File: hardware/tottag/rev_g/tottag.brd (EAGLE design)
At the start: 68.1 x 39.6 mm, 200 parts, among them J1 USB4110-GF-A, J2 DM3AT-SF-PEJM5, J3 TC2030-JLINK-NL-2SIDE, J4 TC2030-JLINK-NL-2SIDE, J5 MOLEX-PICO-SPOX-3SIDE, Q1 CSD75207W15, Q4 CSD75207W15, T1 HHM1595A1, U1 DW1000, U10 STM32F091CC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

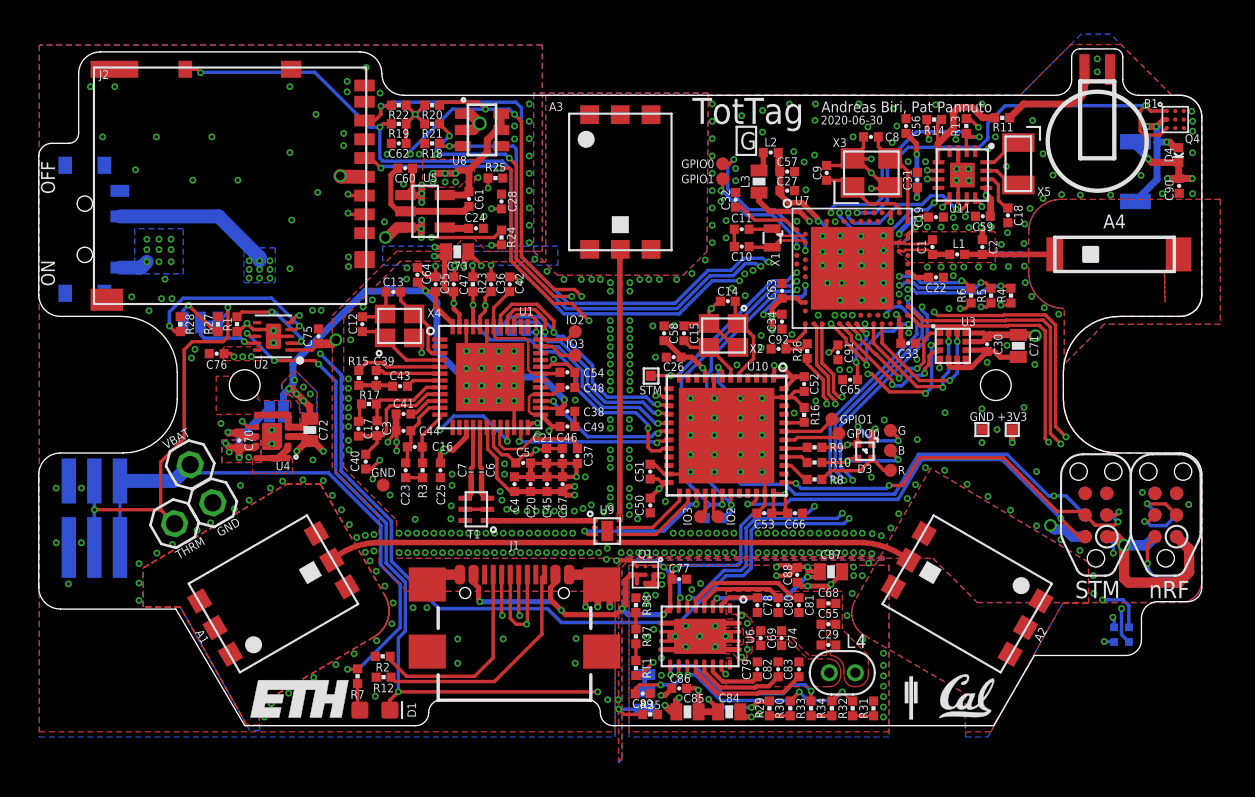
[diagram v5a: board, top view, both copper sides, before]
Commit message: rev_g: renumber R
This script will relabel parts as follows:

R26 : 4.7   0402_RES           => R1 : 4.7   0402_RES

R31 : 97.6   0402_RES          => R2 : 97.6   0402_RES
R32 : 97.6   0402_RES          => R3 : 97.6   0402_RES

R33 : 162   0402_RES           => R4 : 162   0402_RES
R34 : 162   0402_RES           => R5 : 162   0402_RES

R3 : 270   0402_RES            => R6 : 270   0402_RES

R4 : 470   0402_RES            => R7 : 470   0402_RES
R5 : 470   0402_RES            => R8 : 470   0402_RES
R6 : 470   0402_RES            => R9 : 470   0402_RES

R7 : 1k   0402_RES             => R10 : 1k   0402_RES
R8 : 1k   0402_RES             => R11 : 1k   0402_RES
R9 : 1k   0402_RES             => R12 : 1k   0402_RES
R10 : 1k   0402_RES            => R13 : 1k   0402_RES
R37 : 1k   0402_RES            => R14 : 1k   0402_RES
R38 : 1k   0402_RES            => R15 : 1k   0402_RES

R11 : 1.41k   0402_RES         => R16 : 1.41k   0402_RES

R1 : 2.2k   0402_RES           => R17 : 2.2k   0402_RES

R2 : 5.1k   0402_RES           => R18 : 5.1k   0402_RES
R12 : 5.1k   0402_RES          => R19 : 5.1k   0402_RES

R13 : 10k   0402_RES           => R20 : 10k   0402_RES
R27 : 10k   0402_RES           => R21 : 10k   0402_RES
R29 : 10k   0402_RES           => R22 : 10k   0402_RES
R30 : 10k   0402_RES           => R23 : 10k   0402_RES
R35 : 10k   0402_RES           => R24 : 10k   0402_RES

R15 : 11k   0402_RES           => R25 : 11k   0402_RES
R16 : 11k   0402_RES           => R26 : 11k   0402_RES

R17 : 16k   0402_RES           => R27 : 16k   0402_RES

R18 : 100k   0402_RES          => R28 : 100k   0402_RES
R19 : 100k   0402_RES          => R29 : 100k   0402_RES
R20 : 100k   0402_RES          => R30 : 100k   0402_RES
R21 : 100k   0402_RES          => R31 : 100k   0402_RES
R22 : 100k   0402_RES          => R32 : 100k   0402_RES
R23 : 100k   0402_RES          => R33 : 100k   0402_RES
R14 : 100k   0402_RES          => R34 : 100k   0402_RES

R24 : 3.3M   0402_RES          => R35 : 3.3M   0402_RES
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
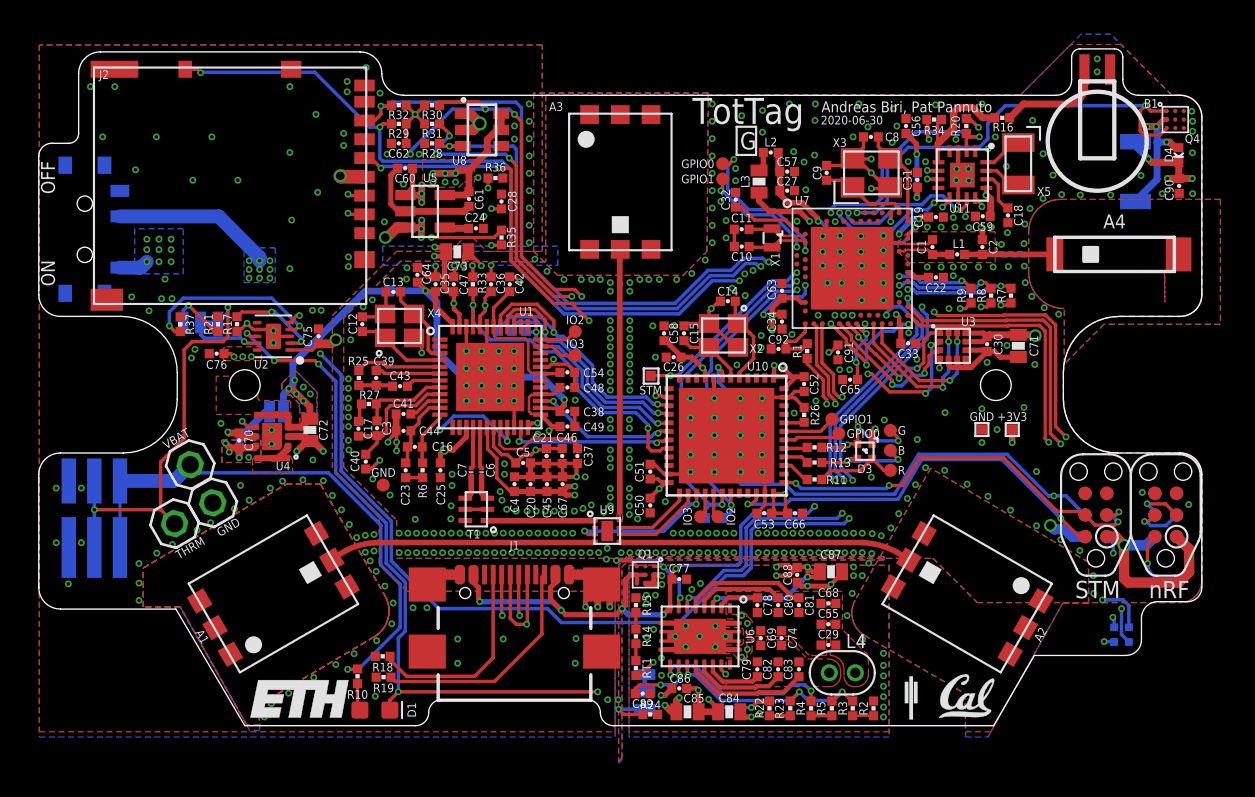
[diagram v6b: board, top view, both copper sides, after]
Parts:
- removed R38: 1k, passives:0402_RES
- added R36: 10M, passives:0402_RES
- R1: value 2.2k -> 4.7
- R11: value 1.41k -> 1k
- R12: value 5.1k -> 1k
- R13: value 10k -> 1k
- R14: value 100k -> 1k
- R15: value 11k -> 1k
- R16: value 11k -> 1.41k
- R17: value 16k -> 2.2k
- R18, R19: value 100k -> 5.1k
- R2: value 5.1k -> 97.6
- R20, R21, R22, R23: value 100k -> 10k
- R24: value 3.3M -> 10k
- R25: value 10M -> 11k
- R26: value 4.7 -> 11k
- R27: value 10k -> 16k
- R28: value DNP -> 100k
- R29, R30: value 10k -> 100k
- R3: value 270 -> 97.6
- R31, R32: value 97.6 -> 100k
- R33, R34: value 162 -> 100k
- R35: value 10k -> 3.3M
- R37: value 1k -> DNP
- R4, R5: value 470 -> 162
- R6: value 470 -> 270
- R7, R8, R9: value 1k -> 470
- moved R7 44.3 mm to (22.9, 18.7), turned to 90 degrees
- moved R32 44.2 mm to (-13.0, 29.9), turned to 0 degrees
- moved R31 42.9 mm to (-11.0, 28.8), turned to 180 degrees
- moved R22 41.5 mm to (8.74, -5.44), turned to 270 degrees
- moved R30 41.1 mm to (-11.0, 29.9), turned to 180 degrees
- moved R29 40.5 mm to (-13.0, 28.8), turned to 0 degrees
- moved R34 35.0 mm to (18.4, 29.1), turned to 180 degrees
- moved R14 35.0 mm to (0.91, -1.22), turned to 270 degrees
- moved R6 33.7 mm to (-11.6, 8.51), turned to 270 degrees
- moved R1 33.4 mm to (10.9, 15.5)
- moved R19 32.4 mm to (-13.9, -3.61), turned to 180 degrees
- moved R37 32.4 mm to (-25.8, 17.1)
- moved R33 31.8 mm to (-8.64, 19.4)
- moved R20 31.3 mm to (20.3, 28.7), turned to 90 degrees
- moved R23 31.0 mm to (9.96, -5.44), turned to 90 degrees
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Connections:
- net !NRF_CS_RTC: now also R34.2; no longer R14.2
- net !NRF_CS_SD: now also R31.1; no longer R21.1
- net !SD_DETECT: now also R29.1; no longer R19.1
- net BATIN: now also R35.1, R36.2; no longer R24.1, R25.2
- net BQ_FOD: now also R23.2, R3.1, R5.2; no longer R30.2, R32.1, R34.2
- net BQ_ILM: now also R4.1; no longer R33.1
- net BQ_RECT: now also R22.1; no longer R29.1
- net DW_IRQ: now also R33.2; no longer R23.2
- net GND: now also R17.1, R19.2, R20.2, R21.1, R24.1, R26.2, R28.2, R33.1, R36.1, R37.1; no longer R1.1, R12.2, R13.2, R16.2, R23.1, R27.1, R28.1, R31.2, R35.1, R38.1
- net LED_BLUE: now also R13.2; no longer R10.2
- net LED_GREEN: now also R12.2; no longer R9.2
- net LED_NRF_BLUE: now also R9.2; no longer R6.2
- net LED_NRF_GREEN: now also R8.2; no longer R5.2
- net LED_NRF_RED: now also R7.2; no longer R4.2
- net LED_RED: now also R11.2; no longer R8.2
- net N$1: now also R19.1; no longer R12.1
- net N$12: now also R27.2; no longer R17.2
- net N$13: now also R18.1; no longer R2.1
- net N$14: now also R6.1; no longer R3.1
- net N$16: now also R27.1; no longer R17.1
- net N$21: now also R25.2; no longer R15.2
- net N$22: now also R26.1; no longer R16.1
- net N$23: now also R12.1; no longer R9.1
- net N$24: now also R13.1; no longer R10.1
- net N$25: now also R11.1; no longer R8.1
- net N$28: now also R2.1, R3.2; no longer R31.1, R32.2
- net N$34: now also R17.2; no longer R1.2
- net N$45: now also R16.2; no longer R11.2
- net N$47: now also R21.2; no longer R27.2
- net N$49: now also R37.2; no longer R28.2
- net N$54: now also R10.2; no longer R7.2
- net N$59: now also R7.1; no longer R4.1
- net N$60: now also R8.1; no longer R5.1
- net N$61: now also R9.1; no longer R6.1
- net N$64: now also R22.2, R23.1; no longer R29.2, R30.1
- net N$66: now also R4.2, R5.1; no longer R33.2, R34.1
- net N$67: now also R24.2; no longer R35.2
- net N$69: now also R14.2; no longer R37.2
- net N$70: now also R14.1, R15.2; no longer R37.1, R38.2
- net N$8: now also R6.2; no longer R3.2
- net NRF_MISO: now also R32.1; no longer R22.1
- net NRF_MOSI: now also R30.1; no longer R20.1
- net RTC_WDI: now also R20.1; no longer R13.1
- net SD_EN: now also R28.1; no longer R18.1
- net VBAT: now also R10.1, R35.2; no longer R24.2, R7.1
- net VBAT_RTC: now also R16.1, R34.1; no longer R11.1, R14.1
- net VCC_SDCARD: now also R29.2, R30.2, R31.2, R32.2; no longer R19.2, R20.2, R21.2, R22.2
- net VUSB: now also R1.1; no longer R26.1
- net VUSB_NRF: now also R1.2; no longer R26.2

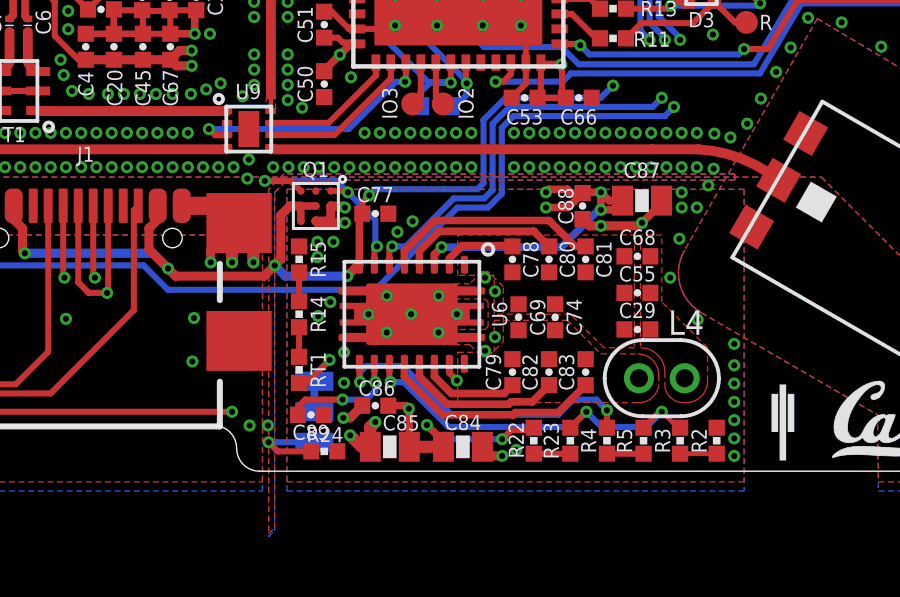
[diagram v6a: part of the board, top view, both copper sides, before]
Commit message: rev_g: fixup airwire I missed in the cap via adding :(
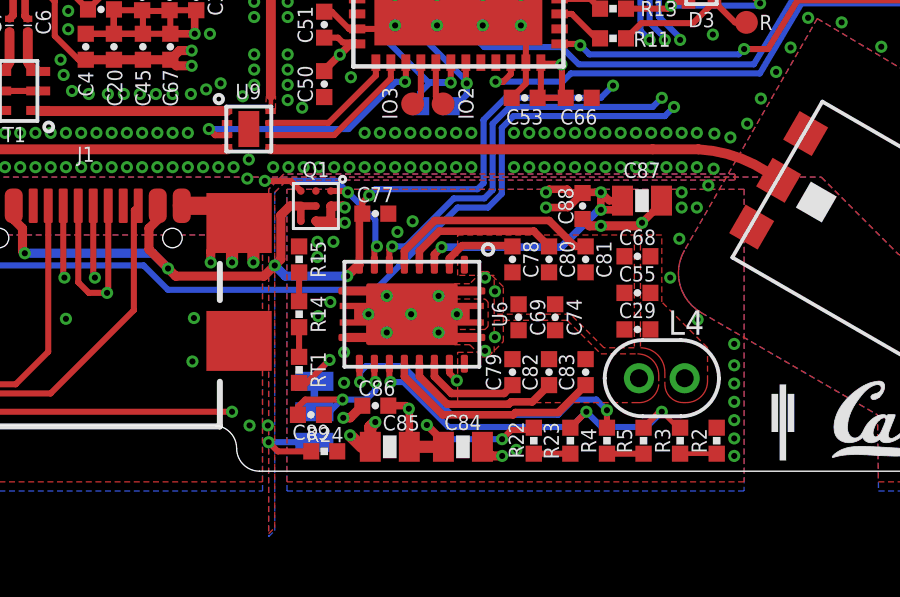
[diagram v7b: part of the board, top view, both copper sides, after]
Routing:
- net QI_TS_CTRL: track 38.2 -> 39.3 mm
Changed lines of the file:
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@@
 <vertex x="7.112" y="-1.7272"/>
 </polygon>
-<wire x1="10.3632" y1="1.95453125" x2="10.44066875" y2="1.95453125" width="0.254" layer="1"/>
 <via x="12.3444" y="1.8288" extent="1-16" drill="0.2032"/>
 <wire x1="12.9944" y1="2.5654" x2="12.9944" y2="2.4788" width="0.254" layer="1"/>
@@
 <wire x1="0.87503125" y1="-4.30656875" x2="1.1176" y2="-4.064" width="0.2032" layer="1"/>
 <wire x1="1.1176" y1="-4.064" x2="2.3622" y2="-4.064" width="0.2032" layer="1"/>
-<wire x1="0.87503125" y1="-4.572" x2="1.4224" y2="-4.4704" width="0" layer="19" extent="1-16"/>
+<wire x1="1.4224" y1="-4.4704" x2="1.9304" y2="-4.4704" width="0.2032" layer="16"/>
+<wire x1="2.3368" y1="-4.064" x2="1.9304" y2="-4.4704" width="0.2032" layer="16"/>
+<wire x1="2.3368" y1="-4.064" x2="2.3622" y2="-4.064" width="0.2032" layer="16"/>
 </signal>
 <signal name="N$67">

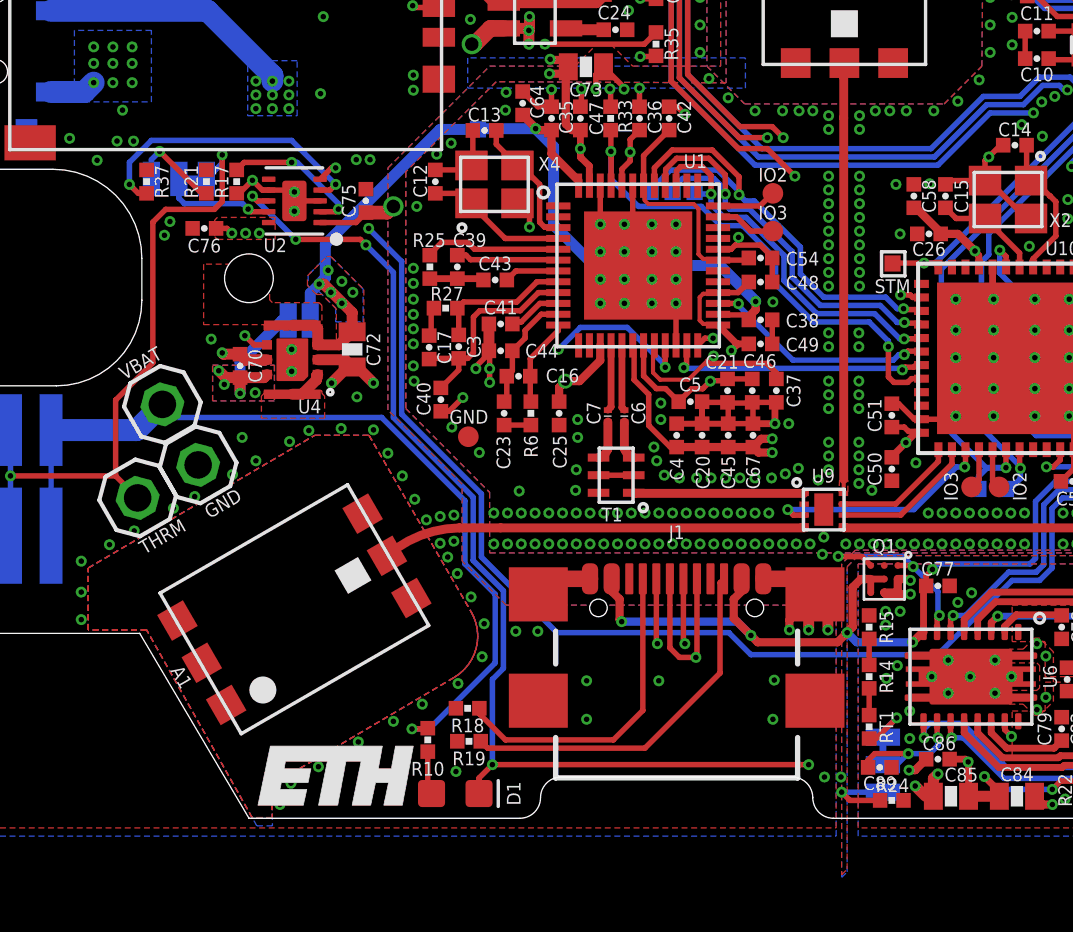
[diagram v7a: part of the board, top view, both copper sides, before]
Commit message: rev_g: add keepouts inside solder jumpers
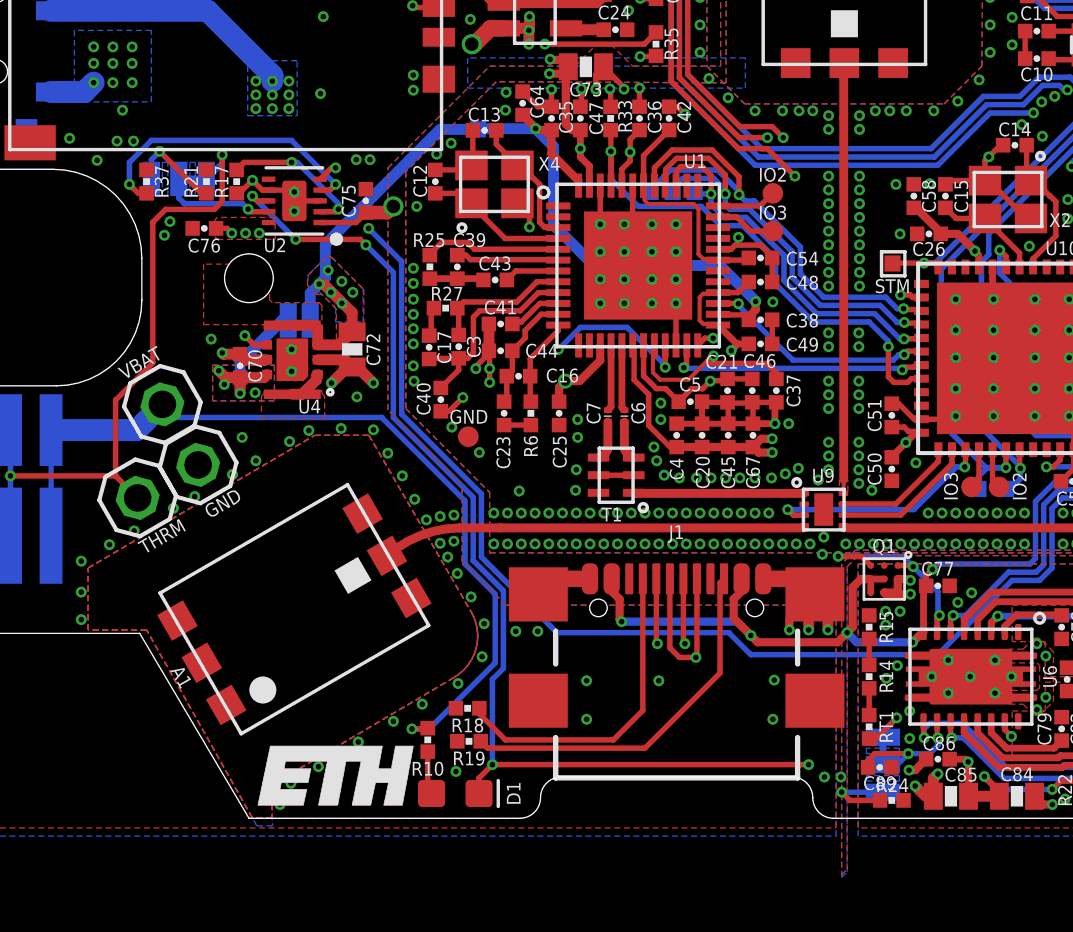
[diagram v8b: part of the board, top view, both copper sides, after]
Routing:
- net QI_TS_CTRL: track 39.3 -> 38.8 mm
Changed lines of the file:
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@@
 <wire x1="10.97333125" y1="1.72666875" x2="12.24226875" y2="1.72666875" width="0.3048" layer="1"/>
 <wire x1="12.24226875" y1="1.72666875" x2="12.3444" y2="1.8288" width="0.3048" layer="1"/>
+<polygon width="0.0254" layer="16" pour="cutout">
+<vertex x="0.8128" y="-4.8768"/>
+<vertex x="0.8128" y="-5.08"/>
+<vertex x="2.032" y="-5.08"/>
+<vertex x="2.032" y="-4.8768"/>
+</polygon>
+<polygon width="0.0254" layer="16" pour="cutout">
+<vertex x="0.8128" y="-3.8608"/>
+<vertex x="0.8128" y="-4.064"/>
+<vertex x="2.032" y="-4.064"/>
+<vertex x="2.032" y="-3.8608"/>
+</polygon>
+<polygon width="0.0254" layer="16" pour="cutout">
+<vertex x="-24.1808" y="16.5608"/>
+<vertex x="-23.9776" y="16.5608"/>
+<vertex x="-23.9776" y="17.78"/>
+<vertex x="-24.1808" y="17.78"/>
+</polygon>
+<polygon width="0.0254" layer="16" pour="cutout">
+<vertex x="-25.1968" y="16.5608"/>
+<vertex x="-24.9936" y="16.5608"/>
+<vertex x="-24.9936" y="17.78"/>
+<vertex x="-25.1968" y="17.78"/>
+</polygon>
 </signal>
 <signal name="VUSB">
@@
 <via x="2.3622" y="-4.064" extent="1-16" drill="0.2032"/>
 <wire x1="3.1496" y1="-4.064" x2="2.3622" y2="-4.064" width="0.2032" layer="16"/>
-<wire x1="1.4224" y1="-4.4704" x2="1.9558" y2="-4.4704" width="0.2032" layer="16"/>
 <via x="15.589" y="17.5954" extent="1-16" drill="0.2032"/>
 <wire x1="15.589" y1="17.5954" x2="15.589" y2="17.7226" width="0.2032" layer="16"/>
@@
 <wire x1="0.87503125" y1="-4.30656875" x2="1.1176" y2="-4.064" width="0.2032" layer="1"/>
 <wire x1="1.1176" y1="-4.064" x2="2.3622" y2="-4.064" width="0.2032" layer="1"/>
-<wire x1="1.4224" y1="-4.4704" x2="1.9304" y2="-4.4704" width="0.2032" layer="16"/>
-<wire x1="2.3368" y1="-4.064" x2="1.9304" y2="-4.4704" width="0.2032" layer="16"/>
-<wire x1="2.3368" y1="-4.064" x2="2.3622" y2="-4.064" width="0.2032" layer="16"/>
+<wire x1="1.4224" y1="-4.4704" x2="1.9558" y2="-4.4704" width="0.2032" layer="16"/>
+<wire x1="1.9558" y1="-4.4704" x2="2.3622" y2="-4.064" width="0.2032" layer="16"/>
 </signal>
 <signal name="N$67">
